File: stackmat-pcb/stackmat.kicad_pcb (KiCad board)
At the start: 2 copper layers, 53.8 x 34.3 mm, 12 parts, among them J1 LCD, J2 RFID, J3 DBG_SERIAL, J4 JACK_MALE, J5 JACK_FEMALE, J7 BTN, J8 Screw_Terminal_01x02, J9 POWER_SW, U1 ESP-12F/E, U2 18650, U3 AMS1117-3.3

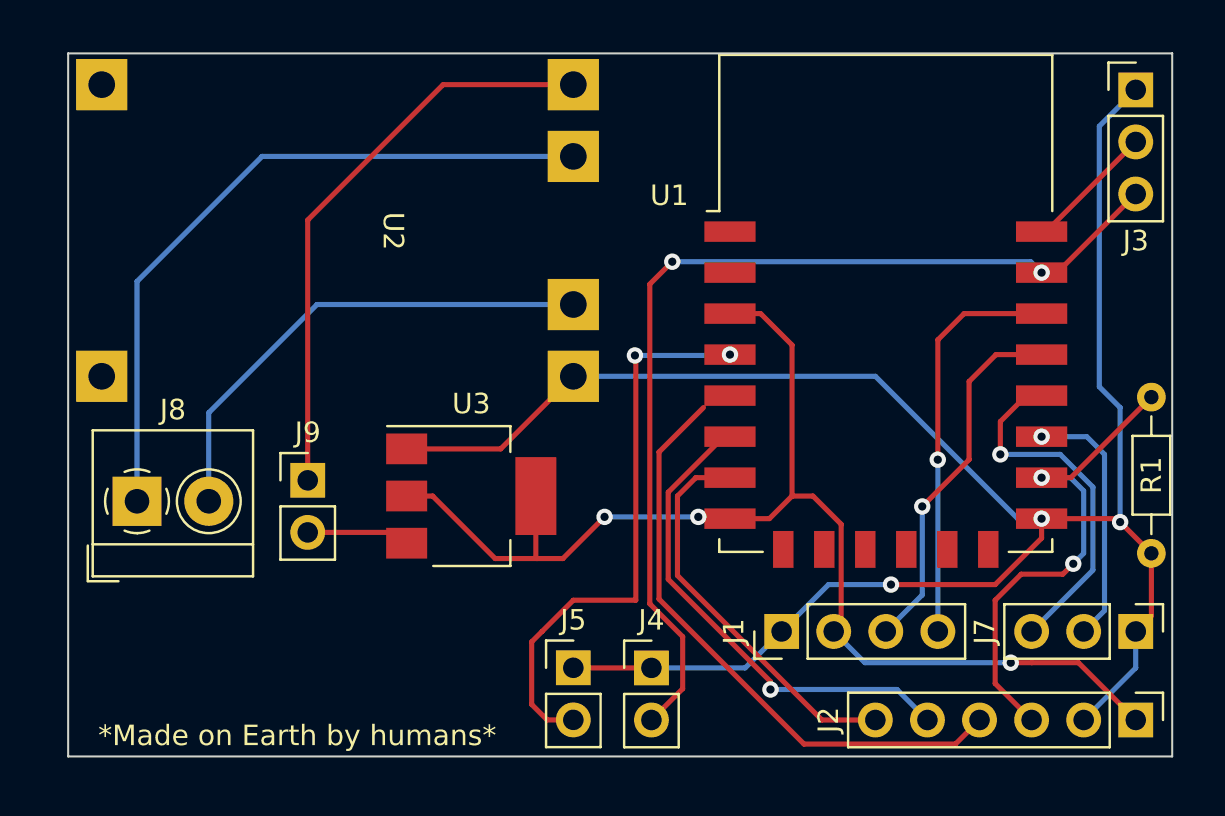
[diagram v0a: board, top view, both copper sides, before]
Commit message: chore: kikit panelizer
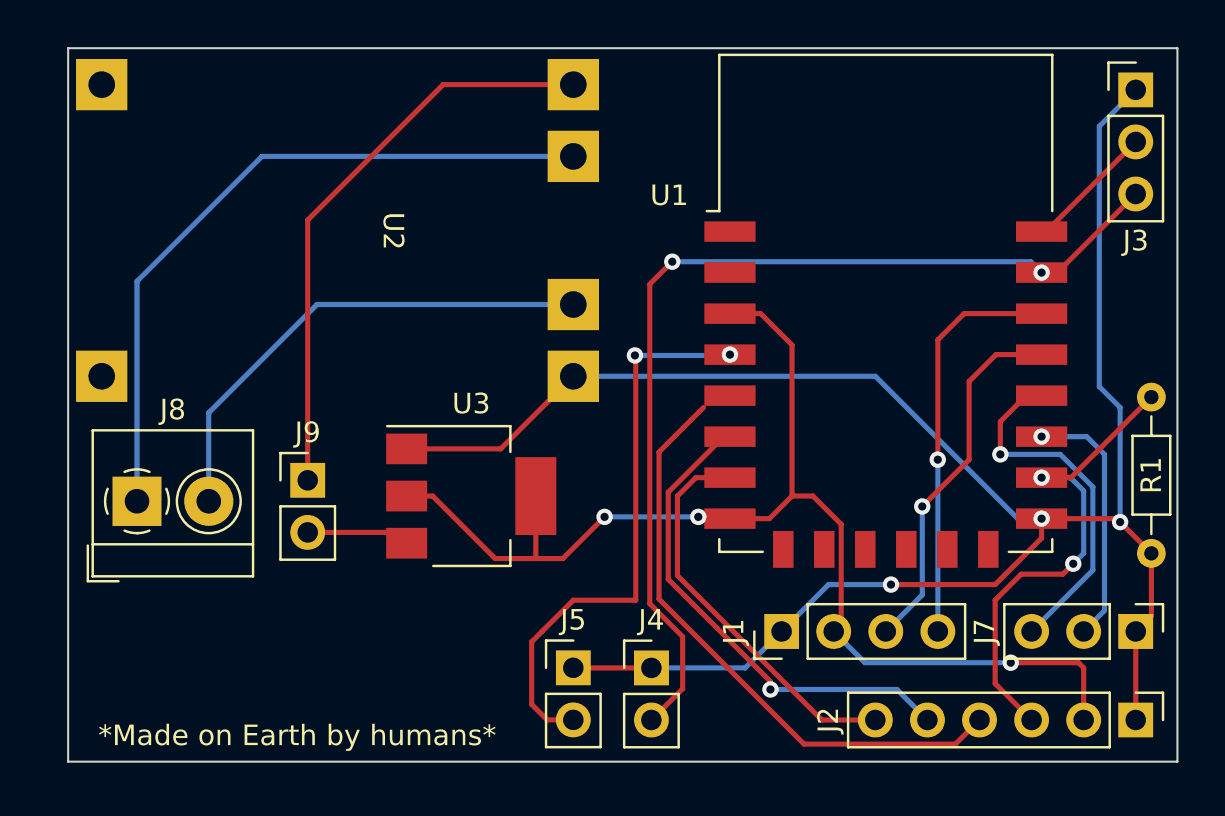
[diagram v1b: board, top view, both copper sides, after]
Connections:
- J2 pad 1: +3.3V -> GND
- J2 pad 2: GND -> +3.3V
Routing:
- net +3.3V: track 60.2 -> 59.1 mm
- net GND: track 99.5 -> 98.5 mm
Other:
- board size 53.8 x 34.3 mm -> 54.1 x 34.8 mm
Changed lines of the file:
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@@
   (net 9 "unconnected-(U1-Pad14)")
   (net 10 "Net-(J1-Pad4)")
-  (net 11 "Net-(U1-Pad4)")
+  (net 11 "Net-(J5-Pad2)")
   (net 12 "Net-(J3-Pad2)")
   (net 13 "Net-(J3-Pad3)")
@@
       (net 1 "GND") (pinfunction "Pin_1") (pintype "passive"))
     (pad "2" thru_hole oval (at 0 2.54) (size 1.7 1.7) (drill 1) (layers *.Cu *.Mask)
-      (net 11 "Net-(U1-Pad4)") (pinfunction "Pin_2") (pintype "passive"))
+      (net 11 "Net-(J5-Pad2)") (pinfunction "Pin_2") (pintype "passive"))
     (model "${KICAD6_3DMODEL_DIR}/Connector_PinHeader_2.54mm.3dshapes/PinHeader_1x02_P2.54mm_Vertical.wrl"
       (offset (xyz 0 0 0))
@@
       (net 25 "+3.3V") (pinfunction "EN") (pintype "input"))
     (pad "4" smd rect (at -7.6 2.5) (size 2.5 1) (layers "F.Cu" "F.Paste" "F.Mask")
-      (net 11 "Net-(U1-Pad4)") (pinfunction "GPIO16") (pintype "bidirectional"))
+      (net 11 "Net-(J5-Pad2)") (pinfunction "GPIO16") (pintype "bidirectional"))
     (pad "5" smd rect (at -7.6 4.5) (size 2.5 1) (layers "F.Cu" "F.Paste" "F.Mask")
       (net 14 "Net-(J2-Pad4)") (pinfunction "GPIO14") (pintype "bidirectional"))
@@
     (fp_line (start 1.27 13.97) (end -1.27 13.97) (layer "F.Fab") (width 0.1))
     (pad "1" thru_hole rect (at 0 0 270) (size 1.7 1.7) (drill 1) (layers *.Cu *.Mask)
-      (net 25 "+3.3V") (pinfunction "Pin_1") (pintype "passive"))
+      (net 1 "GND") (pinfunction "Pin_1") (pintype "passive"))
     (pad "2" thru_hole oval (at 0 2.54 270) (size 1.7 1.7) (drill 1) (layers *.Cu *.Mask)
-      (net 1 "GND") (pinfunction "Pin_2") (pintype "passive"))
+      (net 25 "+3.3V") (pinfunction "Pin_2") (pintype "passive"))
     (pad "3" thru_hole oval (at 0 5.08 270) (size 1.7 1.7) (drill 1) (layers *.Cu *.Mask)
       (net 19 "Net-(J2-Pad3)") (pinfunction "Pin_3") (pintype "passive"))
@@
   (gr_line (start 71.051651 107.317306) (end 71.069488 107.321234) (layer "B.SilkS") (width 0.204153))
   (gr_line (start 70.152826 106.138555) (end 69.503977 106.138555) (layer "B.SilkS") (width 0.239863))
-  (gr_rect (start 66.802 75.184) (end 120.65 109.474) (layer "Edge.Cuts") (width 0.1) (fill none))
+  (gr_rect (start 66.802 74.93) (end 120.904 109.728) (layer "Edge.Cuts") (width 0.1) (fill none))
   (gr_text "*Made on Earth by humans*" (at 77.978 108.458) (layer "F.SilkS")
     (effects (font (size 1 1) (thickness 0.15)))
@@
   (segment (start 119.634 102.616) (end 118.872 103.378) (width 0.25) (layer "F.Cu") (net 1))
   (segment (start 83.312 94.474) (end 87.898 94.474) (width 0.25) (layer "F.Cu") (net 1))
+  (segment (start 118.872 103.378) (end 118.872 107.696) (width 0.25) (layer "F.Cu") (net 1))
   (segment (start 112.014 101.092) (end 114.28 98.826) (width 0.25) (layer "F.Cu") (net 1))
   (segment (start 117.942 97.876) (end 118.11 98.044) (width 0.25) (layer "F.Cu") (net 1))
@@
   (via (at 118.11 98.044) (size 0.8) (drill 0.4) (layers "F.Cu" "B.Cu") (net 1))
   (segment (start 103.886 101.092) (end 106.934 101.092) (width 0.25) (layer "B.Cu") (net 1))
-  (segment (start 118.872 105.156) (end 118.872 103.378) (width 0.25) (layer "B.Cu") (net 1))
   (segment (start 118.11 92.456) (end 118.11 98.044) (width 0.25) (layer "B.Cu") (net 1))
   (segment (start 101.6 103.378) (end 103.886 101.092) (width 0.25) (layer "B.Cu") (net 1))
@@
   (segment (start 117.094 91.44) (end 118.11 92.456) (width 0.25) (layer "B.Cu") (net 1))
   (segment (start 106.172 90.932) (end 113.116 97.876) (width 0.25) (layer "B.Cu") (net 1))
-  (segment (start 116.332 107.696) (end 118.872 105.156) (width 0.25) (layer "B.Cu") (net 1))
   (segment (start 113.116 97.876) (end 114.28 97.876) (width 0.25) (layer "B.Cu") (net 1))
   (segment (start 112.054 89.876) (end 114.28 89.876) (width 0.25) (layer "F.Cu") (net 2))
@@
   (segment (start 100.576 87.876) (end 99.08 87.876) (width 0.25) (layer "F.Cu") (net 25))
   (segment (start 87.63 99.822) (end 84.582 96.774) (width 0.25) (layer "F.Cu") (net 25))
-  (segment (start 116.078 104.902) (end 113.792 104.902) (width 0.25) (layer "F.Cu") (net 25))
+  (segment (start 112.776 104.902) (end 116.078 104.902) (width 0.25) (layer "F.Cu") (net 25))
   (segment (start 84.582 96.774) (end 83.312 96.774) (width 0.25) (layer "F.Cu") (net 25))
   (segment (start 102.108 89.408) (end 100.576 87.876) (width 0.25) (layer "F.Cu") (net 25))
   (segment (start 89.612 99.772) (end 89.612 96.774) (width 0.25) (layer "F.Cu") (net 25))
   (segment (start 92.964 97.79) (end 90.932 99.822) (width 0.25) (layer "F.Cu") (net 25))
-  (segment (start 118.872 107.696) (end 116.078 104.902) (width 0.25) (layer "F.Cu") (net 25))
   (segment (start 89.662 99.822) (end 89.612 99.772) (width 0.25) (layer "F.Cu") (net 25))
   (segment (start 90.932 99.822) (end 89.662 99.822) (width 0.25) (layer "F.Cu") (net 25))
@@
   (segment (start 104.14 103.378) (end 104.505 103.013) (width 0.25) (layer "F.Cu") (net 25))
   (segment (start 99.08 97.876) (end 101.006 97.876) (width 0.25) (layer "F.Cu") (net 25))
+  (segment (start 116.332 105.156) (end 116.332 107.696) (width 0.25) (layer "F.Cu") (net 25))
   (segment (start 104.505 103.013) (end 104.505 98.151) (width 0.25) (layer "F.Cu") (net 25))
+  (segment (start 116.078 104.902) (end 116.332 105.156) (width 0.25) (layer "F.Cu") (net 25))
   (segment (start 101.006 97.876) (end 102.108 96.774) (width 0.25) (layer "F.Cu") (net 25))
   (segment (start 97.536 97.79) (end 98.357604 97.79) (width 0.25) (layer "F.Cu") (net 25))
-  (segment (start 113.792 104.902) (end 112.776 104.902) (width 0.25) (layer "F.Cu") (net 25))
   (segment (start 103.128 96.774) (end 102.108 96.774) (width 0.25) (layer "F.Cu") (net 25))
   (segment (start 102.108 96.774) (end 102.108 89.408) (width 0.25) (layer "F.Cu") (net 25))

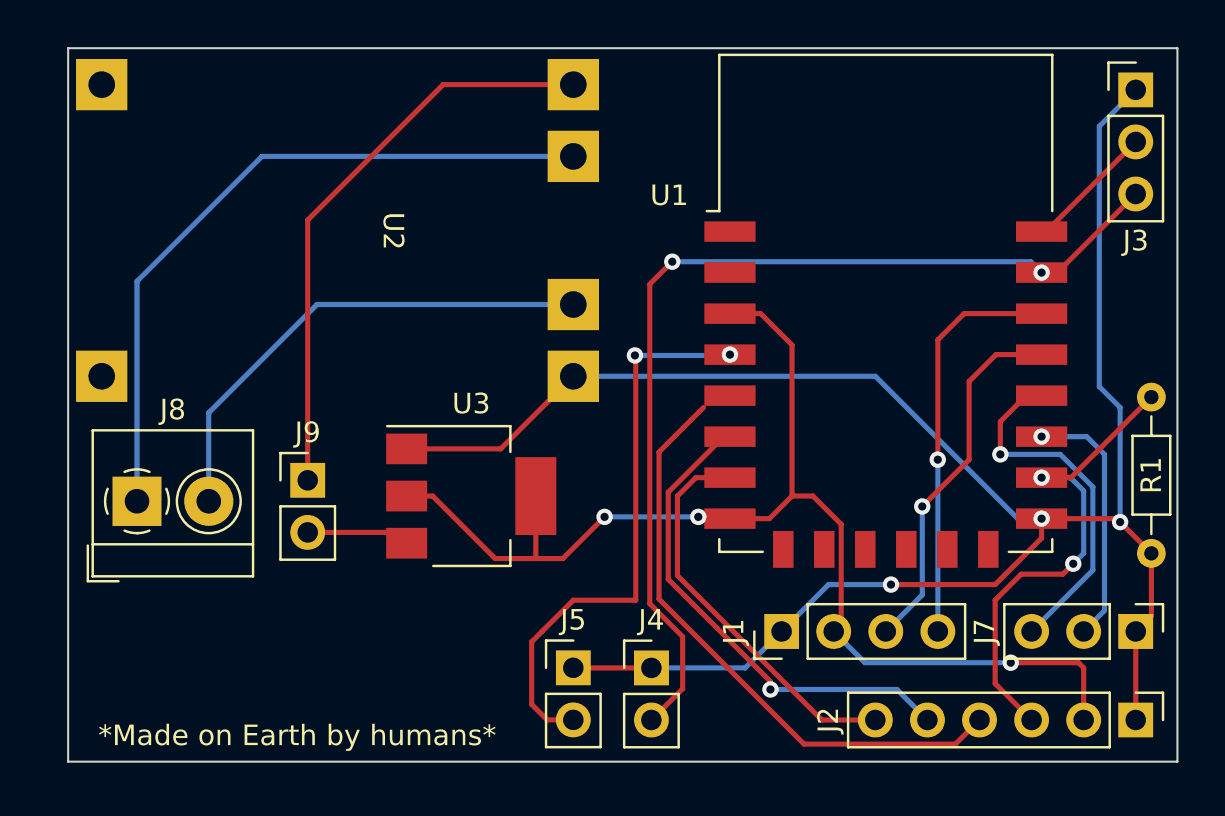
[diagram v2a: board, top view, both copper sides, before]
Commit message: feat: submit time button (with pcb changes)
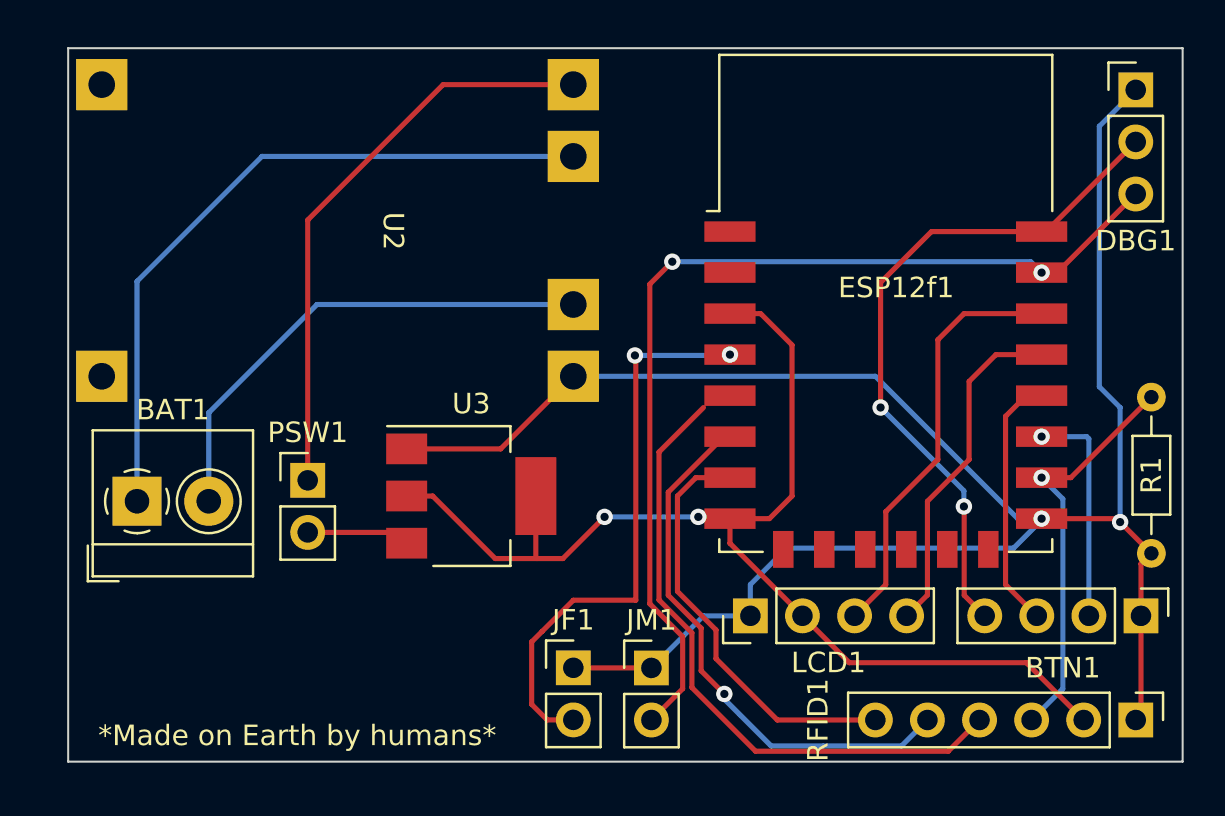
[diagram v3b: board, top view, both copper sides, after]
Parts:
- removed J7: BTN, Connector_PinHeader_2.54mm:PinHeader_1x03_P2.54mm_Vertical
- added BTN1: Conn_01x04, Connector_PinHeader_2.54mm:PinHeader_1x04_P2.54mm_Vertical, F.Cu at (119.1, 102.6)
- moved LCD1 1.70 mm to (100.1, 102.6)
- renumbered J8 to BAT1, J3 to DBG1, U1 to ESP12f1, J5 to JF1, J4 to JM1, J1 to LCD1, J9 to PSW1, J2 to RFID1
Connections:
- ESP12f1 pad 19: Net-(J1-Pin_3) -> Net-(ESP12f1-GPIO4)
- ESP12f1 pad 20: Net-(J1-Pin_4) -> Net-(ESP12f1-GPIO5)
- LCD1 pad 3: Net-(J1-Pin_3) -> Net-(ESP12f1-GPIO5)
- LCD1 pad 4: Net-(J1-Pin_4) -> Net-(ESP12f1-GPIO4)
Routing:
- net Net-(BTN1-Pin_4): track 6.40 -> 33.6 mm, vias 0 -> 2
- net Net-(ESP12f1-GPIO5): track 0.00 -> 20.7 mm
- net Net-(J1-Pin_4): track 19.8 -> 0.00 mm, vias 1 -> 0
- net Net-(J1-Pin_3): track 18.0 -> 0.00 mm, vias 1 -> 0
- net Net-(ESP12f1-GPIO4): track 0.00 -> 16.8 mm
- net Net-(BTN1-Pin_3): track 17.6 -> 12.5 mm, vias 1 -> 0
- net Net-(ESP12f1-GPIO15): track 24.2 -> 19.9 mm, vias 2 -> 1
- net Net-(ESP12f1-GPIO12): track 24.1 -> 26.7 mm
- net Net-(ESP12f1-GPIO14): track 29.3 -> 31.2 mm
- net +3.3V: track 59.1 -> 57.3 mm, vias 3 -> 2
- net Net-(BTN1-Pin_2): track 12.5 -> 11.0 mm
- net Net-(ESP12f1-GPIO13): track 19.4 -> 20.7 mm
- net unconnected-(ESP12f1-ADC-Pad2): track 0.00 -> 0.51 mm
- net GND: track 98.5 -> 98.8 mm, vias 3 -> 2
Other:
- board size 54.1 x 34.8 mm -> 54.4 x 34.8 mm

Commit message: feat(pcb): smaller size (for 2x3 pannels)
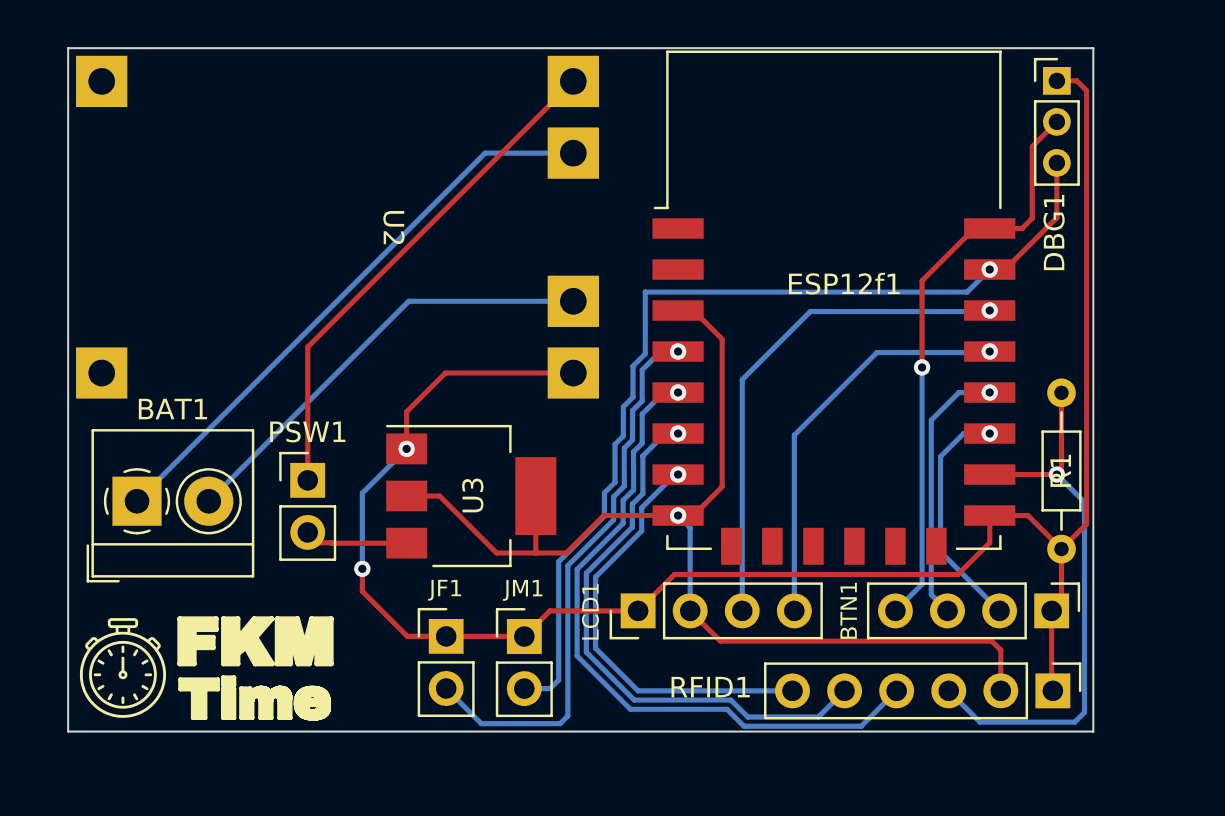
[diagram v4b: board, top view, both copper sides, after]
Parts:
- DBG1: footprint Connector_PinHeader_2.54mm:PinHeader_1x03_P2.54mm_Vertical -> Connector_PinHeader_2.00mm:PinHeader_1x03_P2.00mm_Vertical
- moved JM1 6.39 mm to (89.0, 103.6)
- moved JF1 6.39 mm to (85.2, 103.6)
- moved LCD1 5.48 mm to (94.6, 102.4)
- moved R1 4.39 mm to (115.2, 91.7)
- moved BTN1 4.36 mm to (114.8, 102.4)
- moved RFID1 4.28 mm to (114.8, 106.3)
- moved DBG1 3.87 mm to (115.0, 76.5)
- moved ESP12f1 2.53 mm to (104.2, 87.2)
- moved U2 0.16 mm to (82.2, 83.7)
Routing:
- net GND: track 98.8 -> 89.1 mm
- net Net-(ESP12f1-GPIO15): track 19.9 -> 27.0 mm
- net Net-(BAT1-Pin_1): track 34.5 -> 28.3 mm
- net Net-(BTN1-Pin_4): track 33.6 -> 28.5 mm, vias 2 -> 1
- net Net-(ESP12f1-GPIO5): track 20.7 -> 24.7 mm, vias 0 -> 1
- net +3.3V: track 57.3 -> 53.4 mm, vias 2 -> 1
- net Net-(PSW1-Pin_1): track 28.4 -> 24.8 mm
- net Net-(ESP12f1-GPIO4): track 16.8 -> 19.8 mm, vias 0 -> 1
- net Net-(BAT1-Pin_2): track 24.3 -> 21.8 mm
- net Net-(ESP12f1-GPIO14): track 31.2 -> 33.0 mm, vias 0 -> 1
- net Net-(DBG1-Pin_3): track 48.5 -> 46.8 mm, vias 2 -> 1
- net Net-(ESP12f1-GPIO16): track 27.9 -> 27.3 mm, vias 2 -> 1
- net Net-(BTN1-Pin_2): track 11.0 -> 11.6 mm
- net Net-(ESP12f1-GPIO12): track 26.7 -> 27.3 mm
- net unconnected-(ESP12f1-ADC-Pad2): track 0.51 -> 0.00 mm
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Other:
- board size 54.4 x 34.8 mm -> 50 x 33.3 mm
- board text removed: "*Made on Earth by humans*"

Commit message: feat: disable time offset changes when after submit
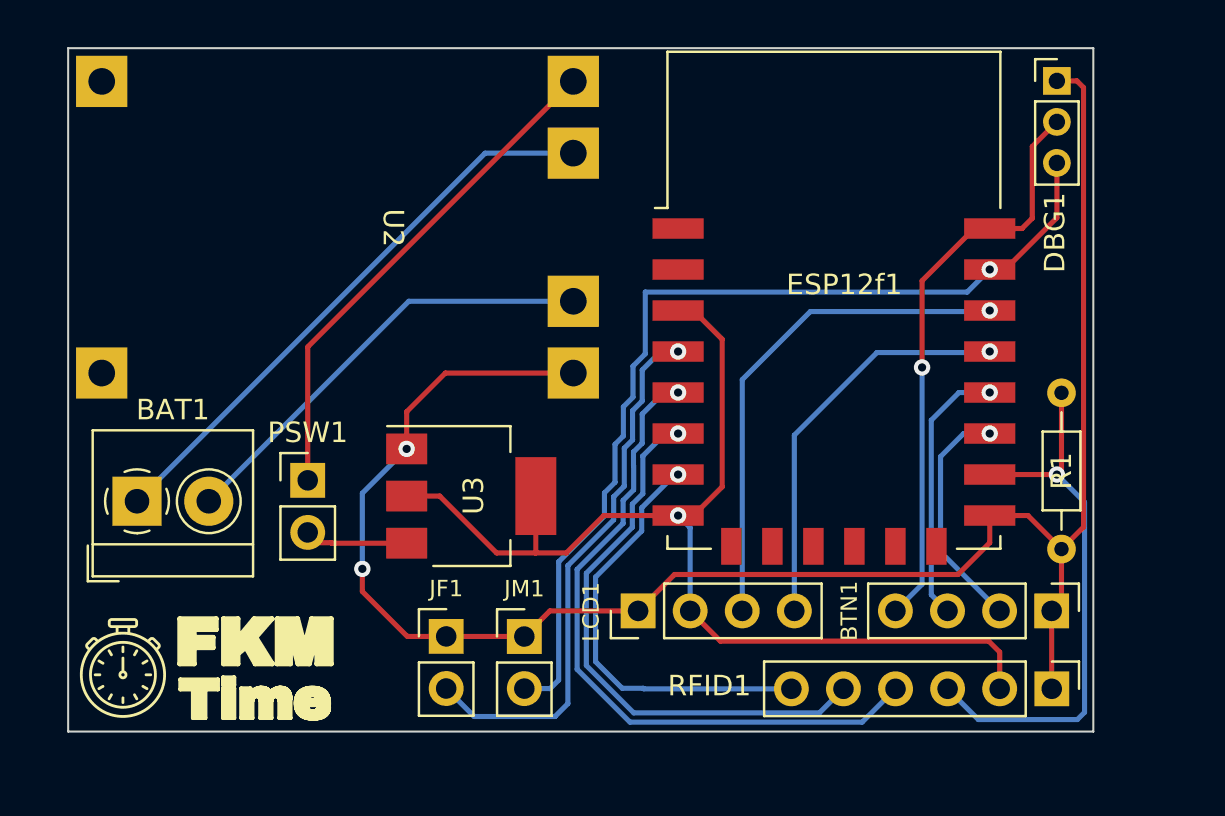
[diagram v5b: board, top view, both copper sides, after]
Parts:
- moved RFID1 0.11 mm to (114.8, 106.2)
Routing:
- net Net-(ESP12f1-GPIO16): track 27.3 -> 26.7 mm
